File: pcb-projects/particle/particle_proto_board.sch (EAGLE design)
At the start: 36 parts, among them IC1 ATTINY20-MMH, IC2 DMC2400V, IC3 DMC2400V

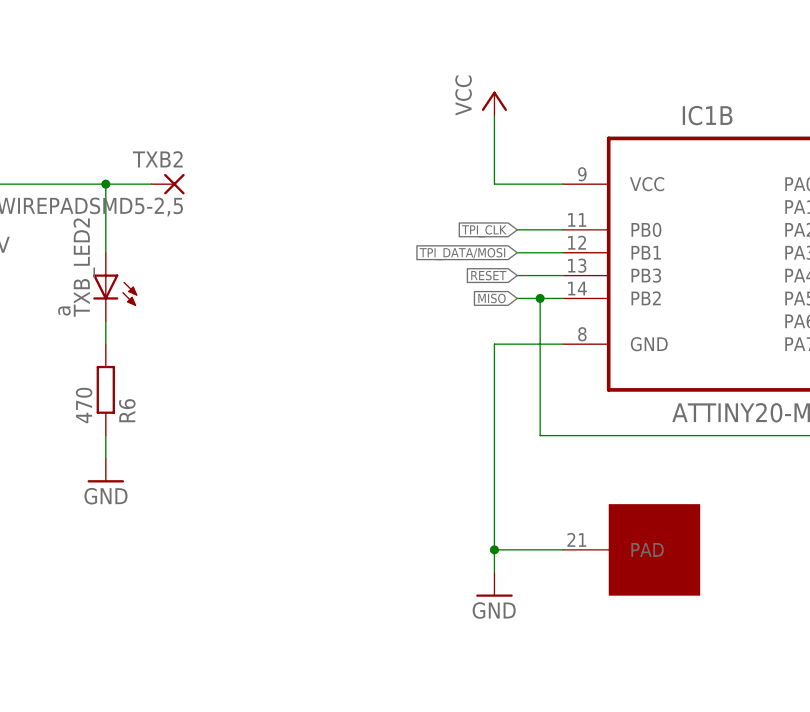
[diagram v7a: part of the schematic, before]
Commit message: fixes #13
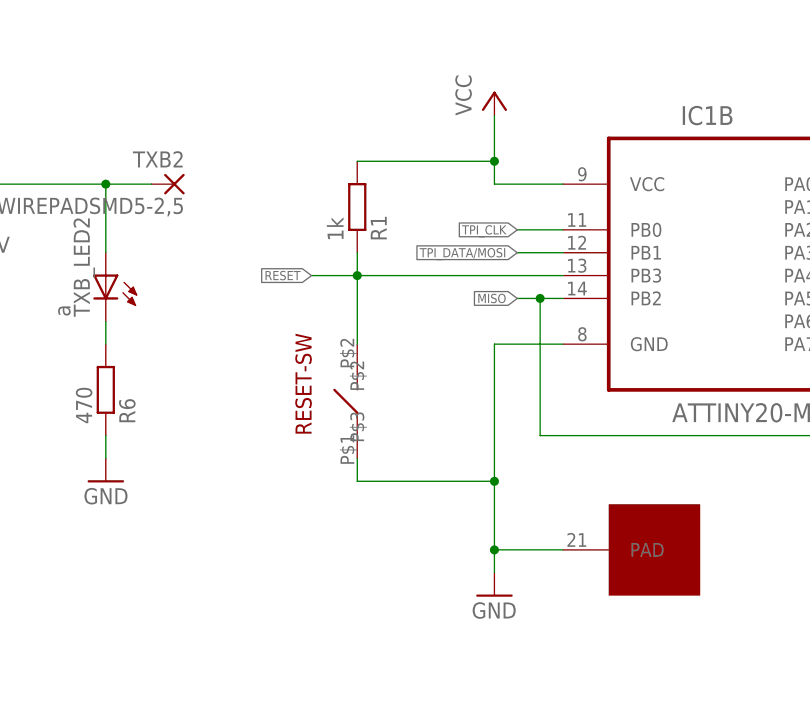
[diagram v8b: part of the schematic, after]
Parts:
- added R1: 1k, rcl:R-EU_R1210
- added RESET-SW: PAD-RESET-SWITCH, reset_pad:PAD-RESET-SWITCH
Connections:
- net GND: now also RESET-SW.P$2
- net RESET: now also R1.1, RESET-SW.P$3
- net VCC: now also R1.2
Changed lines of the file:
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@@
 <layer number="54" name="bGND_GNDA" color="1" fill="9" visible="no" active="no"/>
 <layer number="56" name="wert" color="7" fill="1" visible="no" active="no"/>
+<layer number="90" name="Modules" color="5" fill="1" visible="yes" active="yes"/>
 <layer number="91" name="Nets" color="2" fill="1" visible="yes" active="yes"/>
 <layer number="92" name="Busses" color="1" fill="1" visible="yes" active="yes"/>
@@
 <part name="TPI" library="con-garry" deviceset="332-06" device=""/>
 <part name="SPI" library="con-garry" deviceset="332-06" device=""/>
+<part name="R1" library="rcl" deviceset="R-EU_" device="R1210" value="1k"/>
+<part name="RESET-SW" library="reset_pad" deviceset="PAD-RESET-SWITCH" device=""/>
 </parts>
 <sheets>
@@
 <instance part="SPI" gate="-5" x="124.46" y="-58.42"/>
 <instance part="SPI" gate="-6" x="124.46" y="-68.58"/>
+<instance part="R1" gate="G$1" x="40.64" y="17.78" rot="MR90"/>
+<instance part="RESET-SW" gate="G$1" x="40.64" y="-2.54" rot="R90"/>
 </instances>
 <busses>
@@
 <pinref part="GND13" gate="1" pin="GND"/>
 <wire x1="63.5" y1="2.54" x2="55.88" y2="2.54" width="0.1524" layer="91"/>
-<wire x1="55.88" y1="2.54" x2="55.88" y2="-20.32" width="0.1524" layer="91"/>
+<wire x1="55.88" y1="2.54" x2="55.88" y2="-12.7" width="0.1524" layer="91"/>
 <pinref part="IC1" gate="A" pin="PAD"/>
+<wire x1="55.88" y1="-12.7" x2="55.88" y2="-20.32" width="0.1524" layer="91"/>
 <wire x1="55.88" y1="-20.32" x2="55.88" y2="-22.86" width="0.1524" layer="91"/>
 <wire x1="63.5" y1="-20.32" x2="55.88" y2="-20.32" width="0.1524" layer="91"/>
 <junction x="55.88" y="-20.32"/>
+<pinref part="RESET-SW" gate="G$1" pin="P$2"/>
+<wire x1="40.64" y1="-10.16" x2="40.64" y2="-12.7" width="0.1524" layer="91"/>
+<wire x1="40.64" y1="-12.7" x2="55.88" y2="-12.7" width="0.1524" layer="91"/>
+<junction x="55.88" y="-12.7"/>
 </segment>
 <segment>
@@
 <net name="RESET" class="0">
 <segment>
-<wire x1="63.5" y1="10.16" x2="58.42" y2="10.16" width="0.1524" layer="91"/>
-<label x="58.42" y="10.16" size="1.016" layer="95" rot="R180" xref="yes"/>
+<wire x1="63.5" y1="10.16" x2="40.64" y2="10.16" width="0.1524" layer="91"/>
+<label x="35.56" y="10.16" size="1.016" layer="95" rot="R180" xref="yes"/>
 <pinref part="IC1" gate="B" pin="PB3"/>
+<pinref part="R1" gate="G$1" pin="1"/>
+<wire x1="40.64" y1="10.16" x2="35.56" y2="10.16" width="0.1524" layer="91"/>
+<wire x1="40.64" y1="12.7" x2="40.64" y2="10.16" width="0.1524" layer="91"/>
+<junction x="40.64" y="10.16"/>
+<pinref part="RESET-SW" gate="G$1" pin="P$3"/>
+<wire x1="40.64" y1="10.16" x2="40.64" y2="2.54" width="0.1524" layer="91"/>
 </segment>
 <segment>
@@
 <pinref part="IC1" gate="B" pin="VCC"/>
 <wire x1="63.5" y1="20.32" x2="55.88" y2="20.32" width="0.1524" layer="91"/>
-<wire x1="55.88" y1="20.32" x2="55.88" y2="27.94" width="0.1524" layer="91"/>
+<wire x1="55.88" y1="20.32" x2="55.88" y2="22.86" width="0.1524" layer="91"/>
 <pinref part="P+2" gate="VCC" pin="VCC"/>
-</segment>
-<segment>
+<pinref part="R1" gate="G$1" pin="2"/>
+<wire x1="55.88" y1="22.86" x2="55.88" y2="27.94" width="0.1524" layer="91"/>
+<wire x1="40.64" y1="22.86" x2="55.88" y2="22.86" width="0.1524" layer="91"/>
+<junction x="55.88" y="22.86"/>
+</segment>
+<segment>
